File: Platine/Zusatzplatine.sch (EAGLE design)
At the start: 23 parts

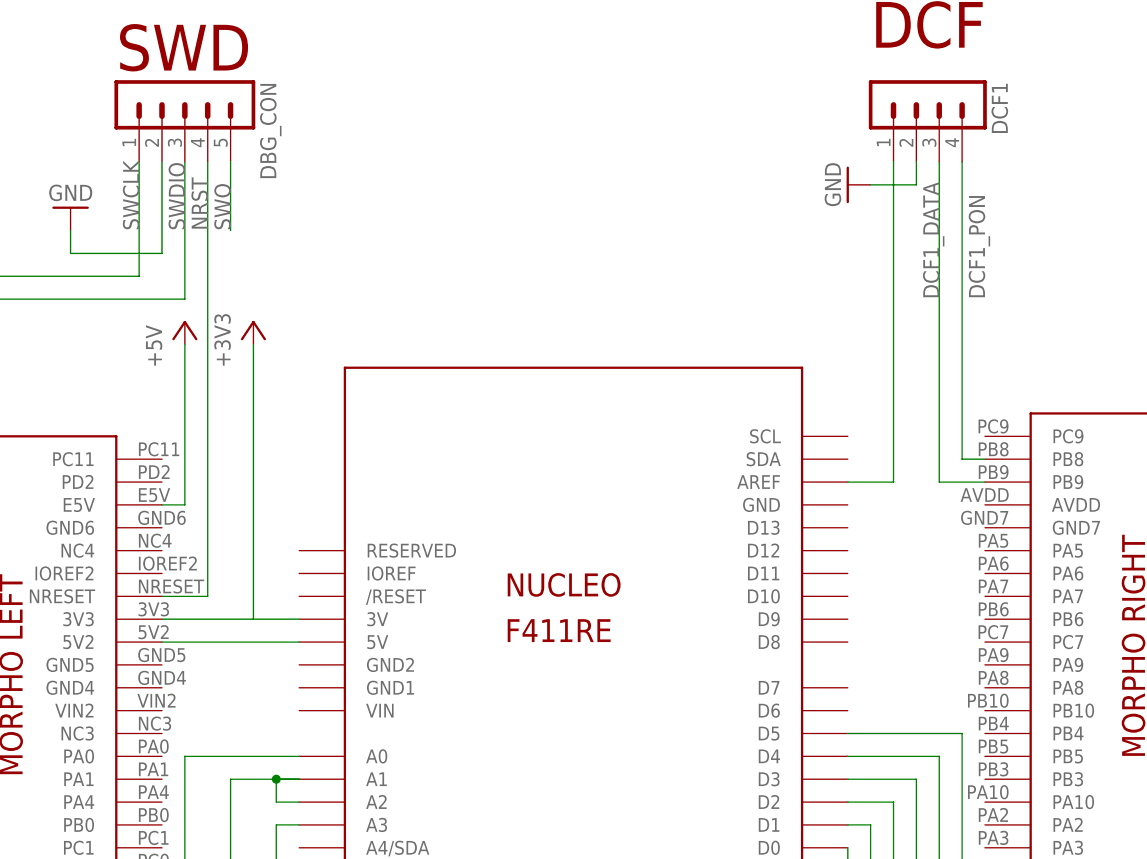
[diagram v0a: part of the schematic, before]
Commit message: Platine: * WS-Schutz Layout verbessert * +5V & GND Leiterbahnen gelöscht (da wir Polygons haben) * DCF-In & DCF-PON auf Arduino Connector verlegt * kleine Trace-Umlegungen um Leitfähigkeit der Polygone zu verbessern * mehrere GND und einen +5V Pin mit entspr. Signalen verbunden
Dokumentation aktualisiert
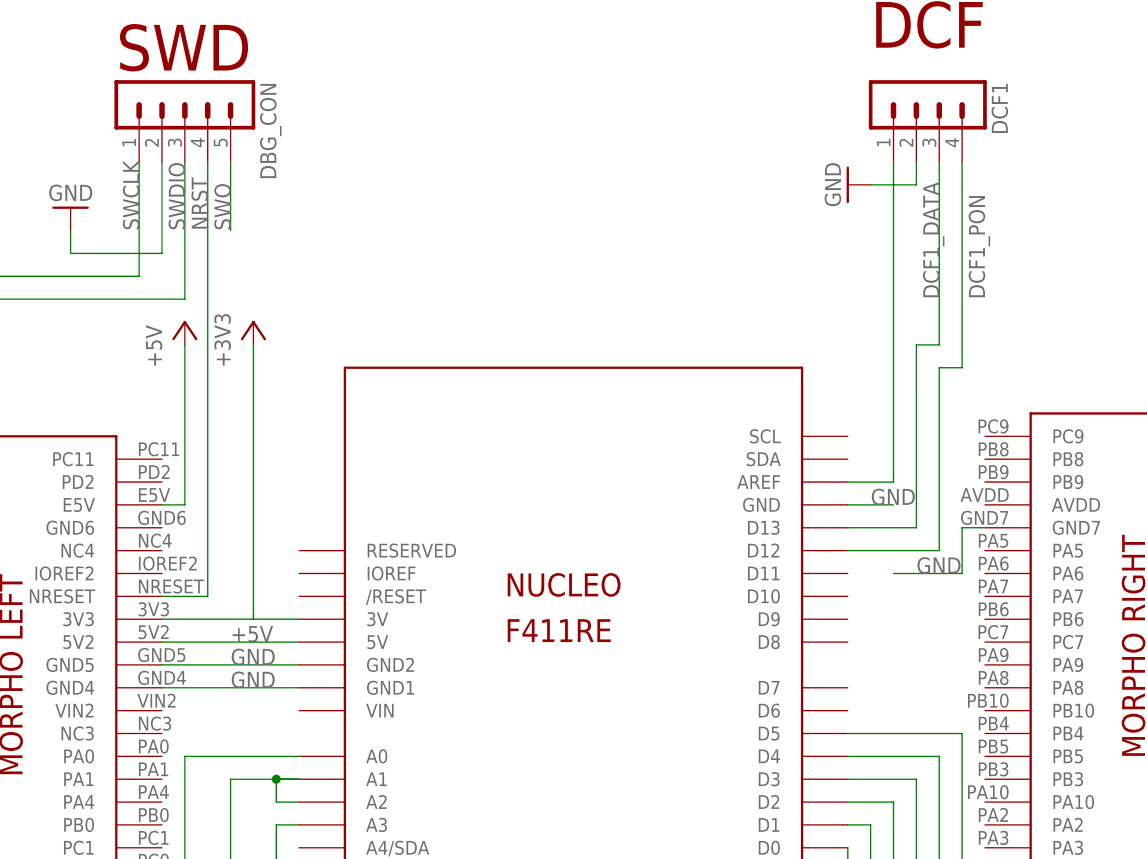
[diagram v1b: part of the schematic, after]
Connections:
- removed net N$2: U$1.5V, U$1.5V2
- net +5V: now also U$1.5V, U$1.5V2
- net DCF1_DATA: now also U$1.D13; no longer U$1.PB9
- net DCF1_PON: now also U$1.D12; no longer U$1.PB8
- net GND: now also U$1.GND, U$1.GND1, U$1.GND2, U$1.GND4, U$1.GND5, U$1.GND7
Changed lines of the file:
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@@
 <?xml version="1.0" encoding="utf-8"?>
 <!DOCTYPE eagle SYSTEM "eagle.dtd">
-<eagle version="7.2.0">
+<eagle version="7.4.0">
 <drawing>
 <settings>
@@
 <pinref part="GND6" gate="1" pin="GND"/>
 </segment>
+<segment>
+<pinref part="U$1" gate="G$1" pin="GND2"/>
+<pinref part="U$1" gate="G$1" pin="GND5"/>
+<wire x1="0" y1="-114.3" x2="-15.24" y2="-114.3" width="0.1524" layer="91"/>
+<label x="-7.62" y="-114.3" size="1.778" layer="95"/>
+</segment>
+<segment>
+<pinref part="U$1" gate="G$1" pin="GND1"/>
+<pinref part="U$1" gate="G$1" pin="GND4"/>
+<wire x1="0" y1="-116.84" x2="-15.24" y2="-116.84" width="0.1524" layer="91"/>
+<label x="-7.62" y="-116.84" size="1.778" layer="95"/>
+</segment>
+<segment>
+<pinref part="U$1" gate="G$1" pin="GND7"/>
+<wire x1="76.2" y1="-99.06" x2="73.66" y2="-99.06" width="0.1524" layer="91"/>
+<wire x1="73.66" y1="-99.06" x2="73.66" y2="-104.14" width="0.1524" layer="91"/>
+<wire x1="73.66" y1="-104.14" x2="66.04" y2="-104.14" width="0.1524" layer="91"/>
+<label x="68.58" y="-104.14" size="1.778" layer="95"/>
+</segment>
+<segment>
+<pinref part="U$1" gate="G$1" pin="GND"/>
+<wire x1="60.96" y1="-96.52" x2="66.04" y2="-96.52" width="0.1524" layer="91"/>
+<label x="63.5" y="-96.52" size="1.778" layer="95"/>
+</segment>
 </net>
 <net name="LED-OUT" class="0">
@@
 <pinref part="PAD_EXT_+5V1" gate="G$1" pin="P"/>
 </segment>
+<segment>
+<pinref part="U$1" gate="G$1" pin="5V2"/>
+<pinref part="U$1" gate="G$1" pin="5V"/>
+<wire x1="-15.24" y1="-111.76" x2="0" y2="-111.76" width="0.1524" layer="91"/>
+<label x="-7.62" y="-111.76" size="1.778" layer="95"/>
+</segment>
 </net>
 <net name="N$8" class="0">
@@
 <segment>
 <pinref part="DCF1" gate="1" pin="4"/>
-<wire x1="73.66" y1="-58.42" x2="73.66" y2="-91.44" width="0.1524" layer="91"/>
+<wire x1="73.66" y1="-58.42" x2="73.66" y2="-81.28" width="0.1524" layer="91"/>
+<wire x1="73.66" y1="-81.28" x2="71.12" y2="-81.28" width="0.1524" layer="91"/>
+<wire x1="71.12" y1="-81.28" x2="71.12" y2="-101.6" width="0.1524" layer="91"/>
 <label x="76.2" y="-73.66" size="1.778" layer="95" rot="R90"/>
-<pinref part="U$1" gate="G$1" pin="PB8"/>
-<wire x1="73.66" y1="-91.44" x2="76.2" y2="-91.44" width="0.1524" layer="91"/>
+<pinref part="U$1" gate="G$1" pin="D12"/>
+<wire x1="71.12" y1="-101.6" x2="60.96" y2="-101.6" width="0.1524" layer="91"/>
 </segment>
 </net>
@@
 <pinref part="DCF1" gate="1" pin="3"/>
 <label x="71.12" y="-73.66" size="1.778" layer="95" rot="R90"/>
-<pinref part="U$1" gate="G$1" pin="PB9"/>
-<wire x1="76.2" y1="-93.98" x2="71.12" y2="-93.98" width="0.1524" layer="91"/>
-<wire x1="71.12" y1="-93.98" x2="71.12" y2="-58.42" width="0.1524" layer="91"/>
+<wire x1="60.96" y1="-99.06" x2="68.58" y2="-99.06" width="0.1524" layer="91"/>
+<wire x1="68.58" y1="-99.06" x2="68.58" y2="-78.74" width="0.1524" layer="91"/>
+<wire x1="68.58" y1="-78.74" x2="71.12" y2="-78.74" width="0.1524" layer="91"/>
+<wire x1="71.12" y1="-78.74" x2="71.12" y2="-58.42" width="0.1524" layer="91"/>
+<pinref part="U$1" gate="G$1" pin="D13"/>
 </segment>
 </net>
@@
 </segment>
 </net>
-<net name="N$2" class="0">
-<segment>
-<pinref part="U$1" gate="G$1" pin="5V2"/>
-<pinref part="U$1" gate="G$1" pin="5V"/>
-<wire x1="-15.24" y1="-111.76" x2="0" y2="-111.76" width="0.1524" layer="91"/>
-</segment>
-</net>
